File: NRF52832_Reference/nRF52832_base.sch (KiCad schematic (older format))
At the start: 22 parts

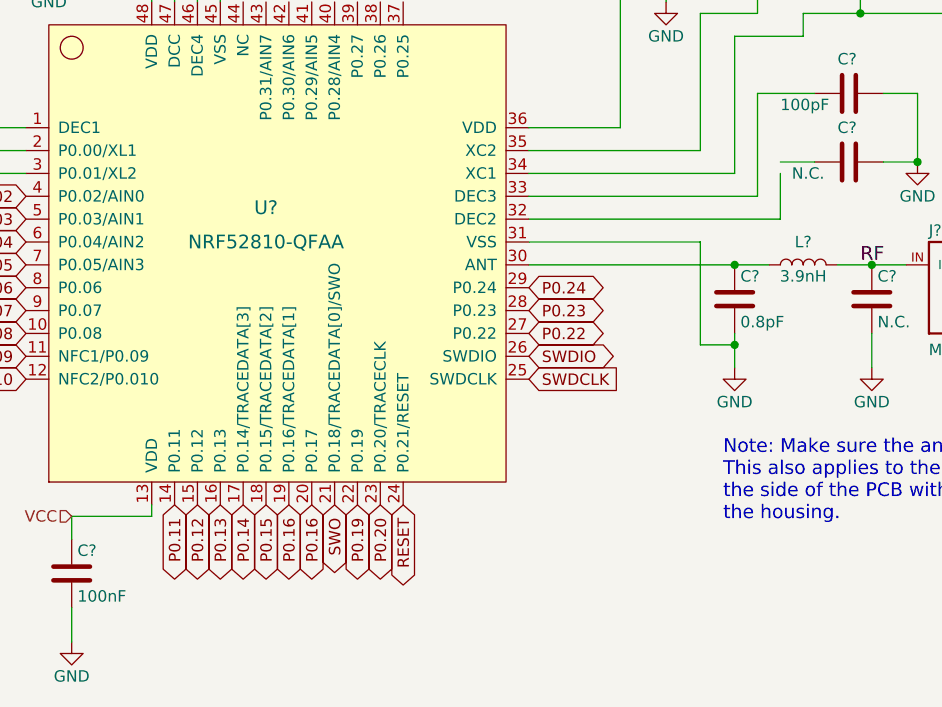
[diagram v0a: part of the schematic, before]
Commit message: Added I2C components: 4KB EEPROM, Light sensor, and Temp sensor to schematic.
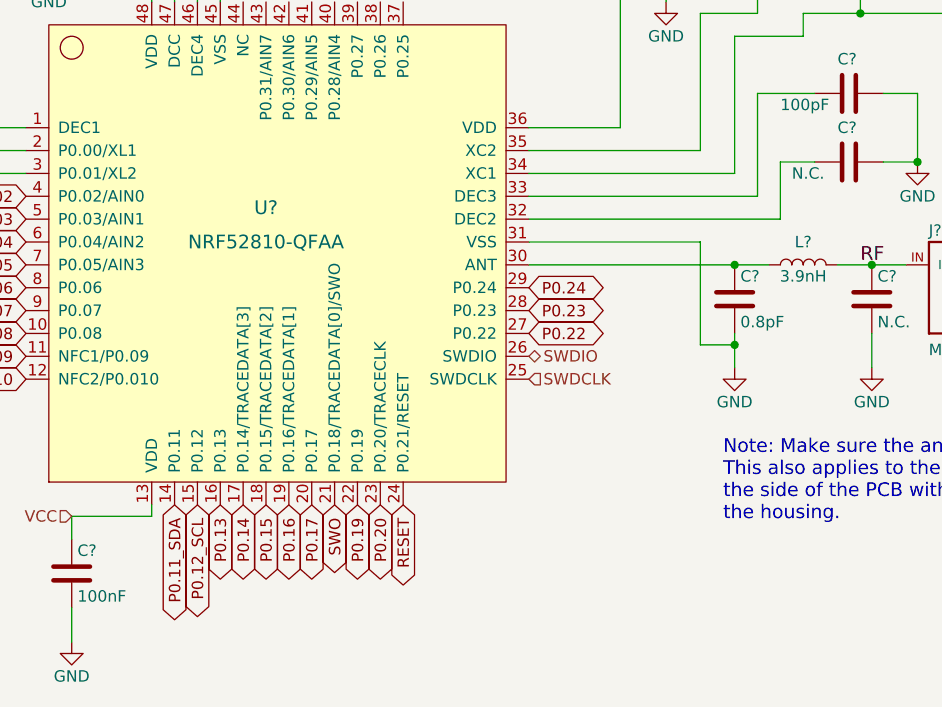
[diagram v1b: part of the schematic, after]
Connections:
- net P0.16: no longer U?.20 (P0.17)
- net at C?.2: now also U?.32 (DEC2)
- net P0.11 renamed P0.11_SDA
- net P0.12 renamed P0.12_SCL
- new net P0.17: U?.20 (P0.17)
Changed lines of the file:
@@
 Connection ~ 7250 4300
-Wire Wire Line
-	7450 3550 7450 3750
 Wire Wire Line
 	7450 3500 7600 3500
@@
 Text GLabel 6350 4250 2    50   BiDi ~ 0
 P0.22
-Text GLabel 6350 4350 2    50   BiDi ~ 0
-SWDIO
-Text GLabel 6350 4450 2    50   Input ~ 0
-SWDCLK
 Text GLabel 4800 5000 3    50   BiDi ~ 0
-P0.11
+P0.11_SDA
 Text GLabel 4900 5000 3    50   BiDi ~ 0
-P0.12
+P0.12_SCL
 Text GLabel 5000 5000 3    50   BiDi ~ 0
 P0.13
@@
 P0.16
 Text GLabel 5400 5000 3    50   BiDi ~ 0
-P0.16
+P0.17
 Text GLabel 5500 5000 3    50   BiDi ~ 0
 SWO
@@
 Text HLabel 6750 2350 0    50   Input ~ 0
 VCC
+Wire Wire Line
+	7450 3500 7450 3750
+Text HLabel 6350 4350 2    50   BiDi ~ 0
+SWDIO
+Text HLabel 6350 4450 2    50   Input ~ 0
+SWDCLK
 $EndSCHEMATC

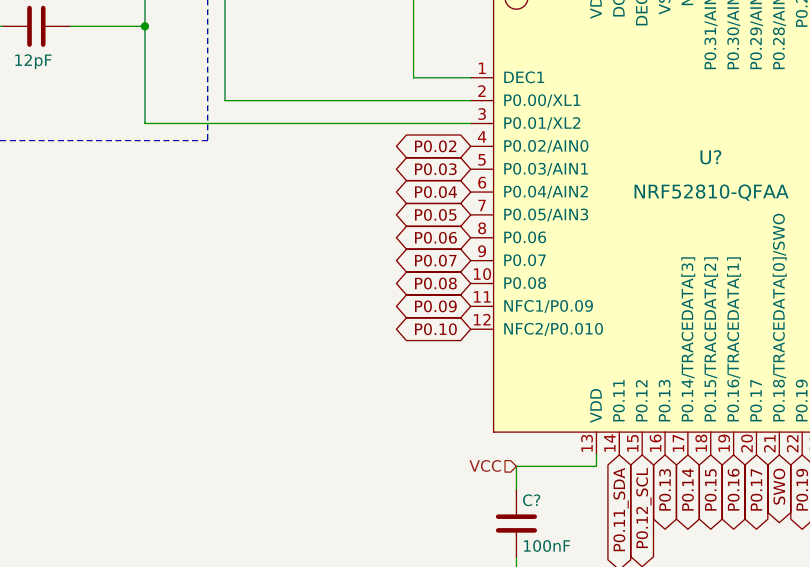
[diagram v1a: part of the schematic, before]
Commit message: Updated LCD circuit schematic.
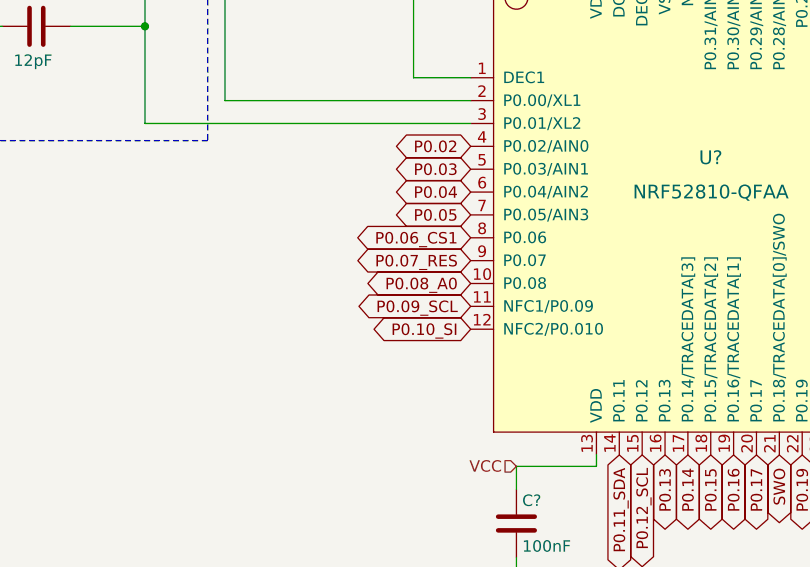
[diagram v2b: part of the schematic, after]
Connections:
- net P0.06 renamed P0.06_CS1
- net P0.07 renamed P0.07_RES
- net P0.08 renamed P0.08_A0
- net P0.09 renamed P0.09_SCL
- net P0.10 renamed P0.10_SI
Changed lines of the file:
@@
 P0.05
 Text GLabel 4150 4050 0    50   BiDi ~ 0
-P0.06
+P0.06_CS1
 Text GLabel 4150 4150 0    50   BiDi ~ 0
-P0.07
+P0.07_RES
 Text GLabel 4150 4250 0    50   BiDi ~ 0
-P0.08
+P0.08_A0
 Text GLabel 4150 4350 0    50   BiDi ~ 0
-P0.09
+P0.09_SCL
 Text GLabel 4150 4450 0    50   BiDi ~ 0
-P0.10
+P0.10_SI
 Text GLabel 6350 4050 2    50   BiDi ~ 0
 P0.24

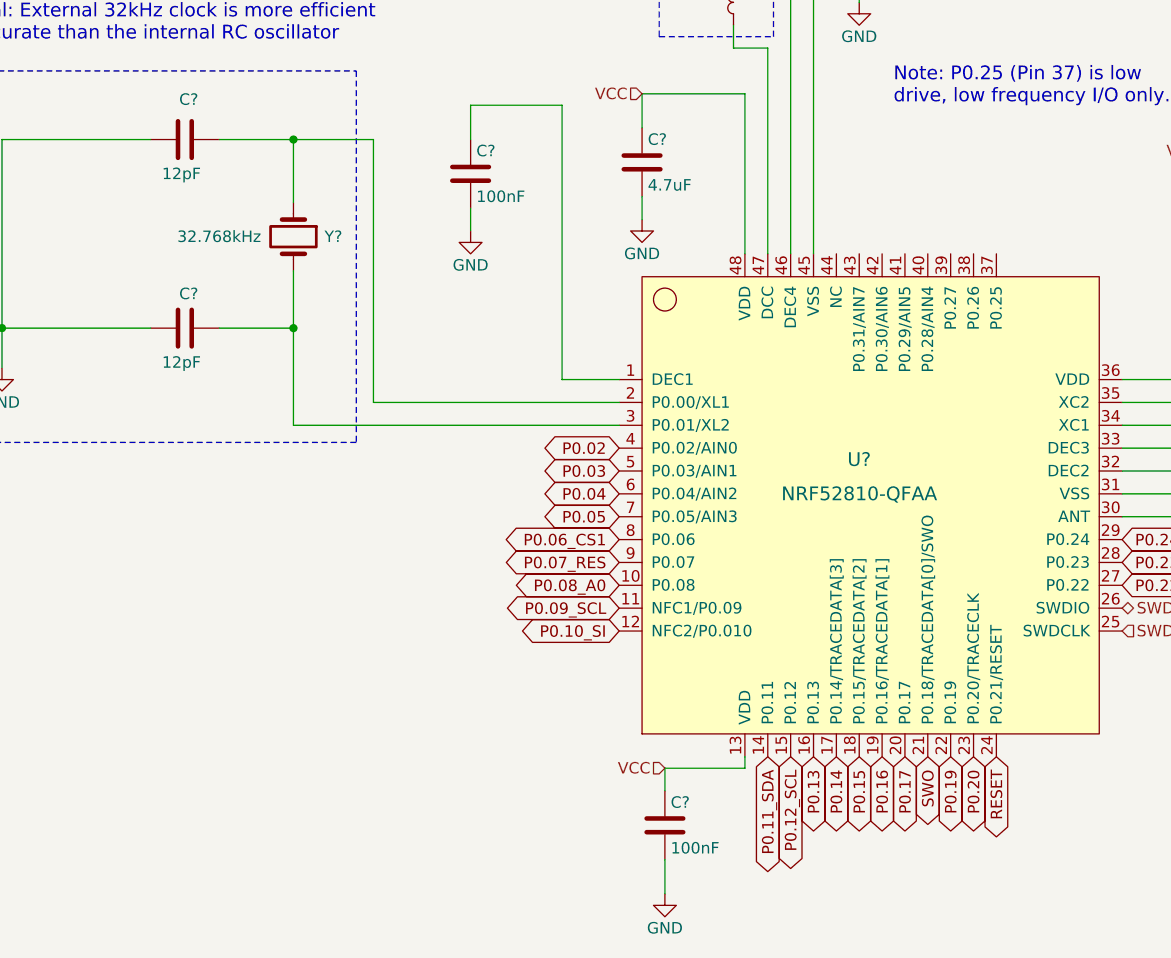
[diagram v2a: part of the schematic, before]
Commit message: Added main power switch and LCD power switch. Added GPIO breakout pins.
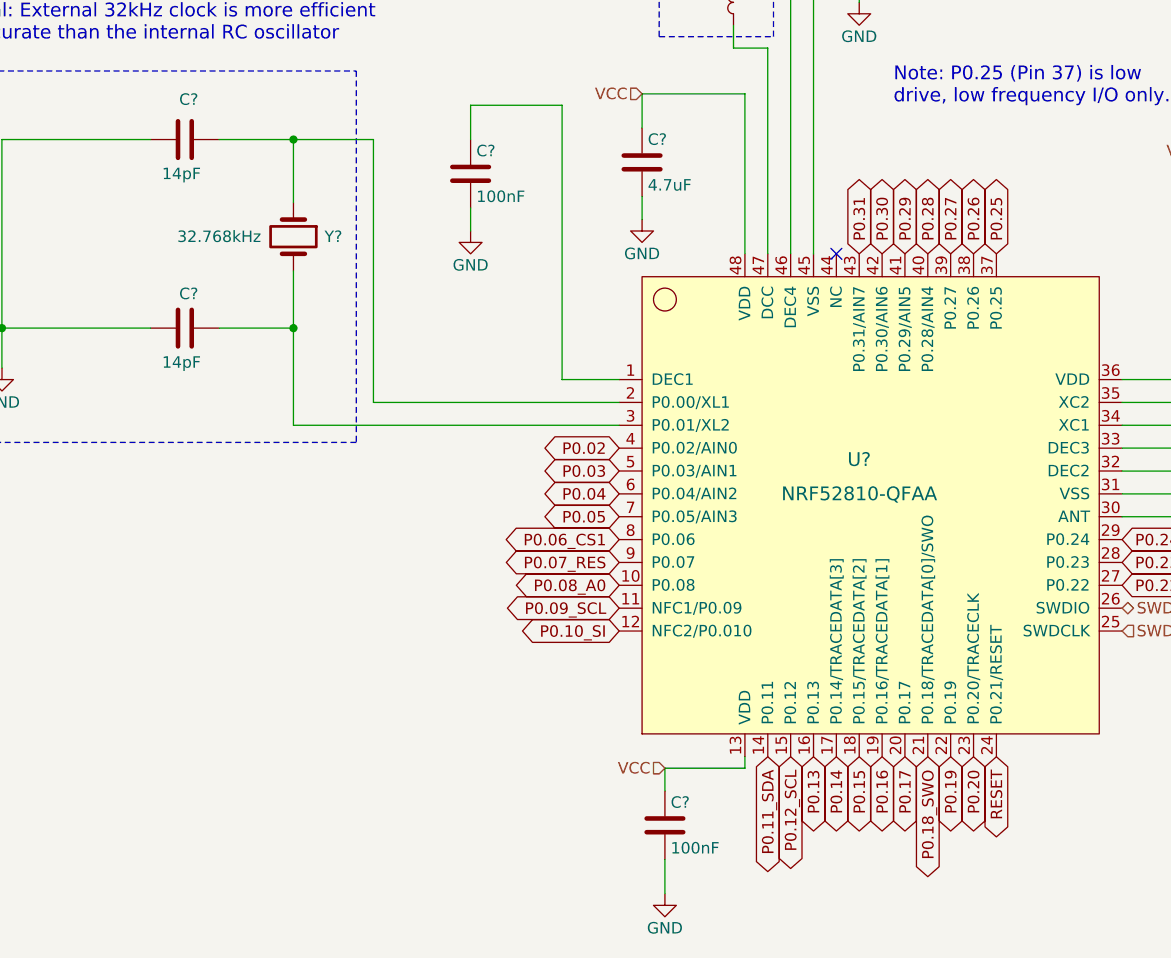
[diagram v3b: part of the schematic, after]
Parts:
- C? (x2): value 12pF -> 14pF
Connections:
- net P0.25: now reaches U?.37 (P0.25)
- net P0.26: now reaches U?.38 (P0.26)
- net P0.27: now reaches U?.39 (P0.27)
- net P0.28: now reaches U?.40 (P0.28/AIN4)
- net P0.29: now reaches U?.41 (P0.29/AIN5)
- net P0.30: now reaches U?.42 (P0.30/AIN6)
- net P0.31: now reaches U?.43 (P0.31/AIN7)
- net SWO renamed P0.18_SWO
- no-connect marks 1 -> 2
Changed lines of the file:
@@
 P 2250 3125
 F 0 "C?" V 2100 3100 50  0000 L CNN
-F 1 "12pF" V 2400 3025 50  0000 L CNN
+F 1 "14pF" V 2400 3025 50  0000 L CNN
 F 2 "Capacitors_SMD:C_0402" H 2288 2975 50  0001 C CNN
 F 3 "" H 2250 3125 50  0001 C CNN
@@
 P 2250 2300
 F 0 "C?" V 2075 2275 50  0000 L CNN
-F 1 "12pF" V 2400 2200 50  0000 L CNN
+F 1 "14pF" V 2400 2200 50  0000 L CNN
 F 2 "Capacitors_SMD:C_0402" H 2288 2150 50  0001 C CNN
 F 3 "" H 2250 2300 50  0001 C CNN
@@
 P0.17
 Text GLabel 5500 5000 3    50   BiDi ~ 0
-SWO
+P0.18_SWO
 Text GLabel 5600 5000 3    50   BiDi ~ 0
 P0.19
@@
 Text HLabel 6350 4450 2    50   Input ~ 0
 SWDCLK
+Text GLabel 5800 2800 1    50   BiDi ~ 0
+P0.25
+Text GLabel 5700 2800 1    50   BiDi ~ 0
+P0.26
+Text GLabel 5600 2800 1    50   BiDi ~ 0
+P0.27
+Text GLabel 5500 2800 1    50   BiDi ~ 0
+P0.28
+Text GLabel 5400 2800 1    50   BiDi ~ 0
+P0.29
+Text GLabel 5300 2800 1    50   BiDi ~ 0
+P0.30
+Text GLabel 5200 2800 1    50   BiDi ~ 0
+P0.31
+NoConn ~ 5100 2800
 $EndSCHEMATC

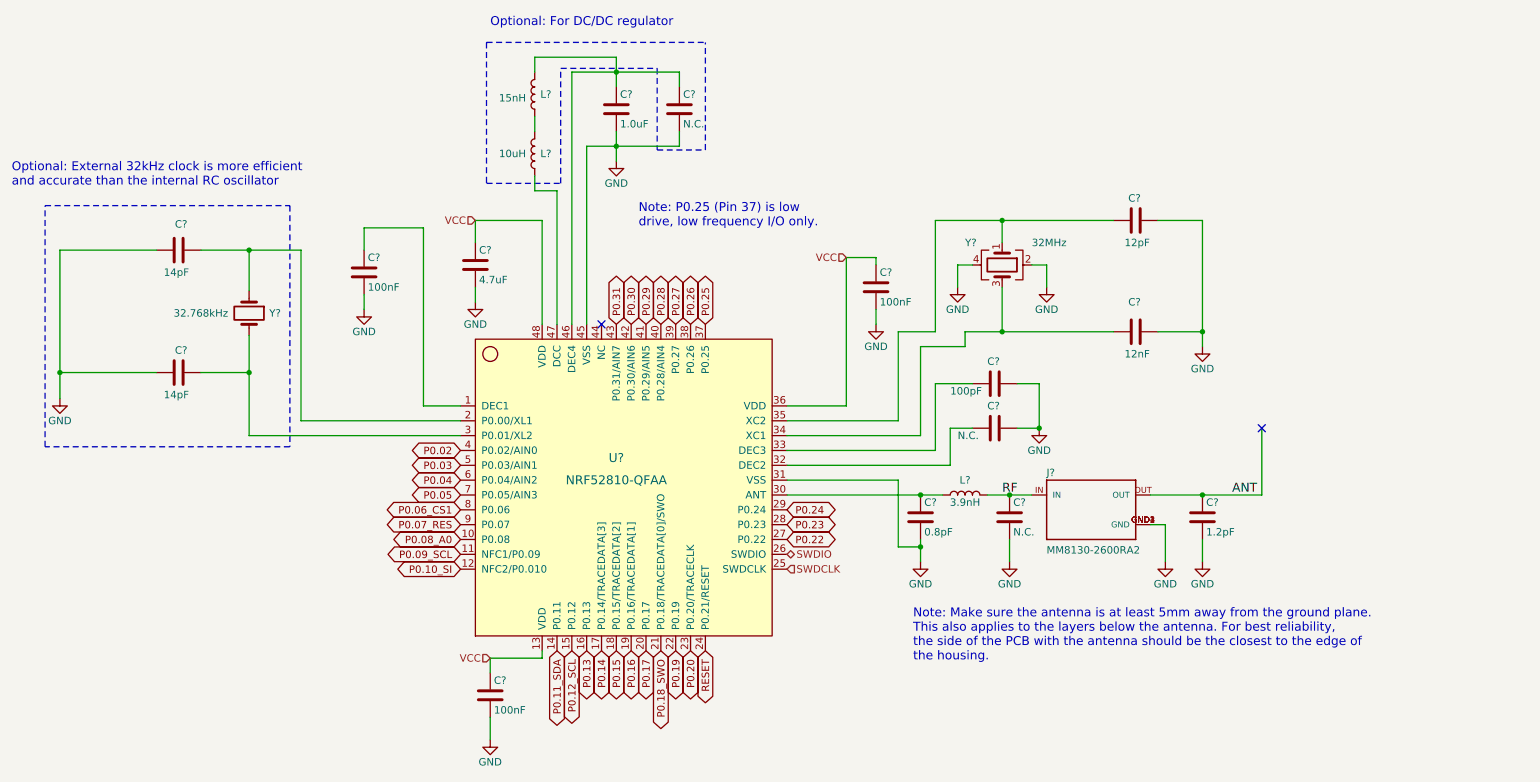
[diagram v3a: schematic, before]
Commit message: Finished footprint assignments for NRF52 base components
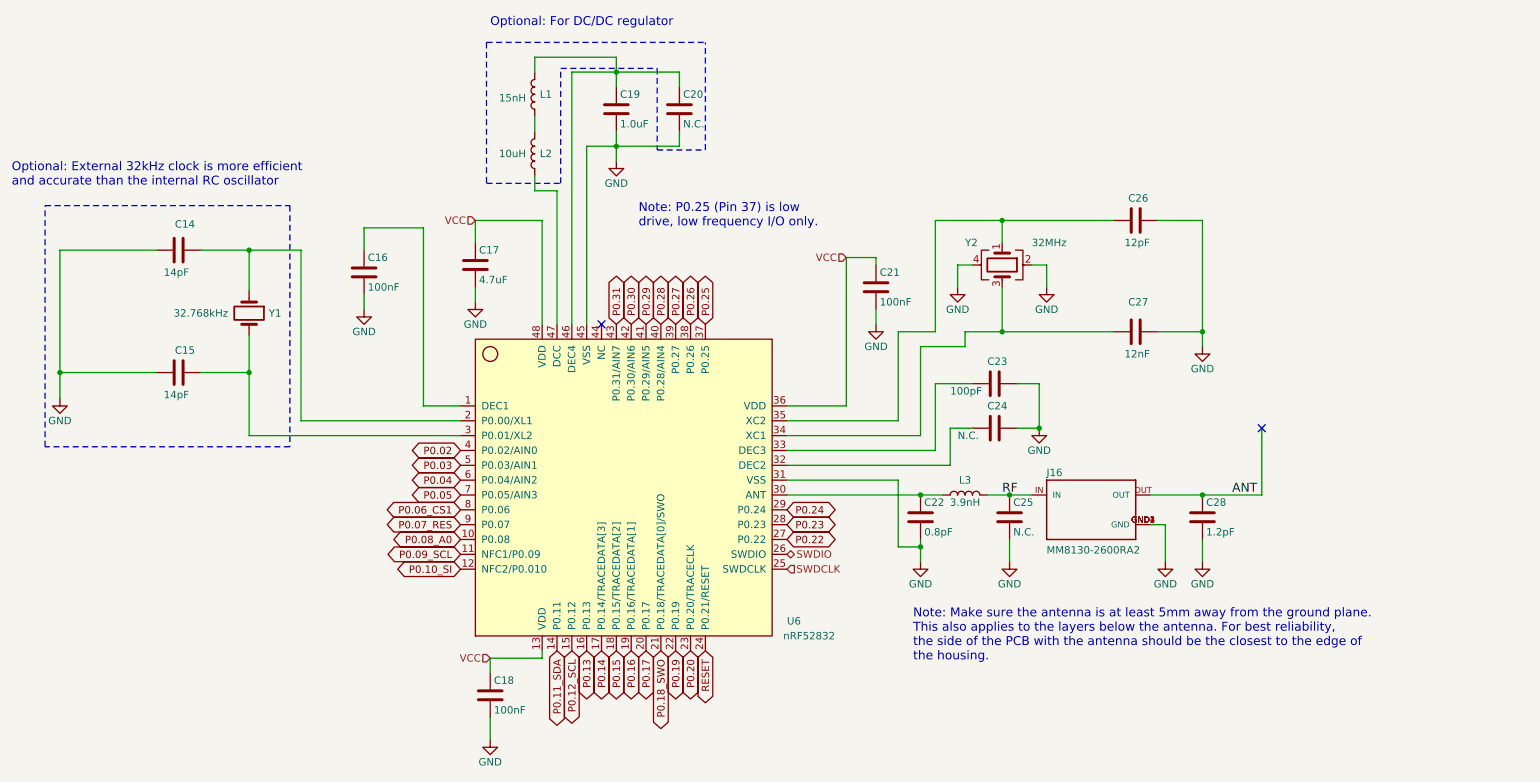
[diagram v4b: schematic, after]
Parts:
- removed U?: NRF52810-QFAA, Package_DFN_QFN:QFN-48-1EP_6x6mm_P0.4mm_EP4.66x4.66mm_ThermalVias, symbol Project_Libary:nRF52832
- added U6: nRF52832, Package_DFN_QFN:QFN-48-1EP_6x6mm_P0.4mm_EP4.3x4.3mm_ThermalVias, symbol Project_Libary:nRF52832
- C14, C15, C16, C18, C21, C22, C23, C24, C25, C26, C27, C28: renamed from C?; footprint Capacitors_SMD:C_0402 -> Capacitor_SMD:C_0402_1005Metric
- C17, C19: renamed from C?; footprint Capacitors_SMD:C_0603 -> Capacitor_SMD:C_0603_1608Metric
- C20: renamed from C?; footprint Capacitors_SMD:C_0402 -> Capacitor_SMD:C_0603_1608Metric
- L1, L3: renamed from L?; footprint Inductors_SMD:L_0402 -> Inductor_SMD:L_0402_1005Metric
- L2: renamed from L?; footprint Inductors_SMD:L_0603 -> Inductor_SMD:L_0603_1608Metric
- Y1: renamed from Y?; footprint Crystals:Crystal_SMD_3215-2pin_3.2x1.5mm -> Crystal:Crystal_SMD_3215-2Pin_3.2x1.5mm
- Y2: renamed from Y?; footprint Crystals:Crystal_SMD_2016-4pin_2.0x1.6mm -> Custom_Footprints:Crystal_32MHz_Kyocera_CX3225SB32000D0FFFCC
- gave numbers to parts that had none: 1
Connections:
- net GND: now also U6.31 (VSS), U6.45 (VSS)
- net P0.02: now also U6.4 (P0.02/AIN0)
- net P0.03: now also U6.5 (P0.03/AIN1)
- net P0.04: now also U6.6 (P0.04/AIN2)
- net P0.05: now also U6.7 (P0.05/AIN3)
- net P0.06_CS1: now also U6.8 (P0.06)
- net P0.07_RES: now also U6.9 (P0.07)
- net P0.08_A0: now also U6.10 (P0.08)
- net P0.09_SCL: now also U6.11 (NFC1/P0.09)
- net P0.10_SI: now also U6.12 (NFC2/P0.010)
- net P0.11_SDA: now also U6.14 (P0.11)
- net P0.12_SCL: now also U6.15 (P0.12)
- net P0.13: now also U6.16 (P0.13)
- net P0.14: now also U6.17 (P0.14/TRACEDATA[3])
- net P0.15: now also U6.18 (P0.15/TRACEDATA[2])
- net P0.16: now also U6.19 (P0.16/TRACEDATA[1])
- net P0.17: now also U6.20 (P0.17)
- net P0.18_SWO: now also U6.21 (P0.18/TRACEDATA[0]/SWO)
- net P0.19: now also U6.22 (P0.19)
- net P0.20: now also U6.23 (P0.20/TRACECLK)
- net P0.22: now also U6.27 (P0.22)
- net P0.23: now also U6.28 (P0.23)
- net P0.24: now also U6.29 (P0.24)
- net P0.25: now also U6.37 (P0.25)
- net P0.26: now also U6.38 (P0.26)
- net P0.27: now also U6.39 (P0.27)
- net P0.28: now also U6.40 (P0.28/AIN4)
- net P0.29: now also U6.41 (P0.29/AIN5)
- net P0.30: now also U6.42 (P0.30/AIN6)
- net P0.31: now also U6.43 (P0.31/AIN7)
- net RESET: now also U6.24 (P0.21/RESET)
- net SWDCLK: now also U6.25 (SWDCLK)
- net SWDIO: now also U6.26 (SWDIO)
- net VCC: now also U6.13 (VDD), U6.36 (VDD), U6.48 (VDD)
- net at C22.1, L3.1: now also U6.30 (ANT)
- net at C24.2: now also U6.32 (DEC2)
- net at C23.2: now also U6.33 (DEC3)
- net at C16.1: now also U6.1 (DEC1)
- net at C19.1, C20.1, L1.2: now also U6.46 (DEC4)
- net at L2.1: now also U6.47 (DCC)
- net at C26.2, Y2.1: now also U6.35 (XC2)
- net at C27.2, Y2.3: now also U6.34 (XC1)
- net at C15.1, Y1.2: now also U6.3 (P0.01/XL2)
- net at C14.1, Y1.1: now also U6.2 (P0.00/XL1)

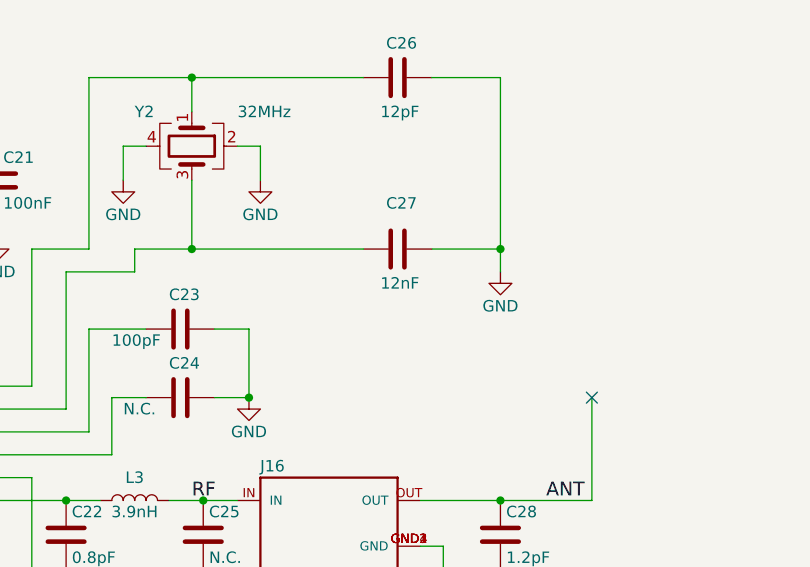
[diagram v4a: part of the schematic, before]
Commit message: Fixed wrong values for some components
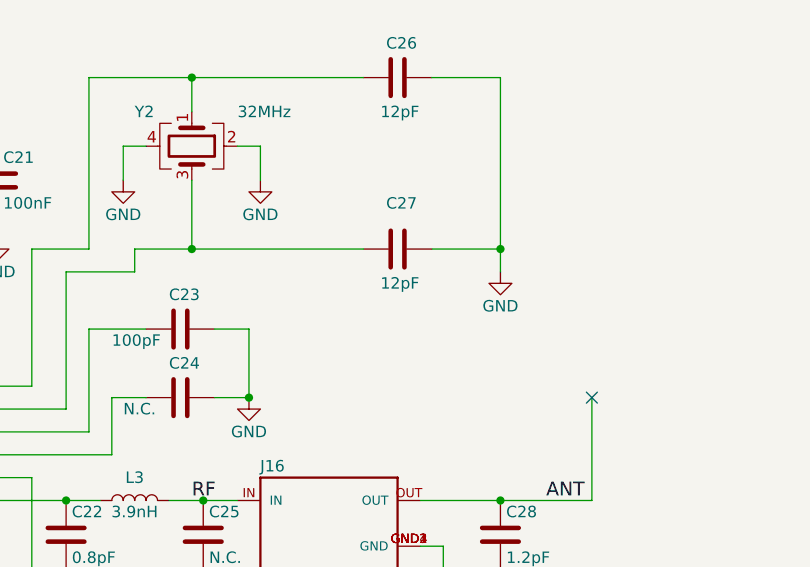
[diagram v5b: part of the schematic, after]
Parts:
- C27: value 12nF -> 12pF
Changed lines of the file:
@@
 P 8700 2850
 F 0 "C27" V 8500 2800 50  0000 L CNN
-F 1 "12nF" V 8850 2775 50  0000 L CNN
+F 1 "12pF" V 8850 2775 50  0000 L CNN
 F 2 "Capacitor_SMD:C_0402_1005Metric" H 8738 2700 50  0001 C CNN
 F 3 "" H 8700 2850 50  0001 C CNN

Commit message: Updating rescue lib for NRF52 Reference.
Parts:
- U6: symbol Project_Libary:nRF52832 -> NRF52832_Reference-rescue:nRF52832-Project_Libary
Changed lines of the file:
@@
 NoConn ~ 5100 2800
 $Comp
-L Project_Libary:nRF52832 U6
+L NRF52832_Reference-rescue:nRF52832-Project_Libary U6
 U 1 1 5C28BD1C
 P 5000 4450
+AR Path="/5C28BD1C" Ref="U6"  Part="1"
+AR Path="/5BF15572/5C28BD1C" Ref="U6"  Part="1"
 F 0 "U6" H 6350 4100 50  0000 L CNN
 F 1 "nRF52832" H 6325 4000 50  0000 L CNN
